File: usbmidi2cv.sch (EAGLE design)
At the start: 33 parts, among them IC1 LM324N

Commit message: melhorias na pcb
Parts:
- R5: device pot:TRIM_EU-B64W -> rcl:R-TRIMM3006P
- renumbered CONTROL_CHANGE to CTRL_CHANGE
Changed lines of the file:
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@@
 <part name="NOTE" library="solpad" library_urn="urn:adsk.eagle:library:364" deviceset="LSP10" device="" package3d_urn="urn:adsk.eagle:package:26501/1"/>
 <part name="SUPPLY4" library="supply2" library_urn="urn:adsk.eagle:library:372" deviceset="GND" device=""/>
-<part name="CONTROL_CHANGE" library="solpad" library_urn="urn:adsk.eagle:library:364" deviceset="LSP10" device="" package3d_urn="urn:adsk.eagle:package:26501/1"/>
+<part name="CTRL_CHANGE" library="solpad" library_urn="urn:adsk.eagle:library:364" deviceset="LSP10" device="" package3d_urn="urn:adsk.eagle:package:26501/1"/>
 <part name="IC1" library="linear" library_urn="urn:adsk.eagle:library:262" deviceset="LM324" device="N" package3d_urn="urn:adsk.eagle:package:16407/2"/>
 <part name="R4" library="rcl" library_urn="urn:adsk.eagle:library:334" deviceset="R-EU_" device="0207/12" package3d_urn="urn:adsk.eagle:package:23489/1" value="10k"/>
 <part name="SUPPLY6" library="supply2" library_urn="urn:adsk.eagle:library:372" deviceset="GND" device=""/>
-<part name="R5" library="pot" library_urn="urn:adsk.eagle:library:331" deviceset="TRIM_EU-" device="B64W" package3d_urn="urn:adsk.eagle:package:22686/1" value="2k"/>
+<part name="R5" library="rcl" library_urn="urn:adsk.eagle:library:334" deviceset="R-TRIMM" device="3006P" package3d_urn="urn:adsk.eagle:package:23758/1" value="2k"/>
 <part name="R6" library="rcl" library_urn="urn:adsk.eagle:library:334" deviceset="R-EU_" device="0207/12" package3d_urn="urn:adsk.eagle:package:23489/1" value="6k8"/>
 <part name="PSU_+12V" library="solpad" library_urn="urn:adsk.eagle:library:364" deviceset="LSP10" device="" package3d_urn="urn:adsk.eagle:package:26501/1"/>
@@
 </instance>
 <instance part="SUPPLY4" gate="GND" x="-25.4" y="68.58" smashed="yes"/>
-<instance part="CONTROL_CHANGE" gate="1" x="55.88" y="-5.08" smashed="yes" rot="R270">
+<instance part="CTRL_CHANGE" gate="1" x="55.88" y="-5.08" smashed="yes" rot="R270">
 <attribute name="NAME" x="59.69" y="-4.699" size="1.778" layer="95"/>
 </instance>
@@
 </instance>
 <instance part="SUPPLY6" gate="GND" x="30.48" y="30.48" smashed="yes"/>
-<instance part="R5" gate="1" x="35.56" y="38.1" smashed="yes" rot="R90">
+<instance part="R5" gate="G$1" x="35.56" y="38.1" smashed="yes" rot="R90">
 <attribute name="VALUE" x="36.83" y="34.29" size="1.778" layer="96" rot="R180"/>
 </instance>
@@
 <segment>
 <pinref part="IC1" gate="D" pin="OUT"/>
-<pinref part="CONTROL_CHANGE" gate="1" pin="MP"/>
+<pinref part="CTRL_CHANGE" gate="1" pin="MP"/>
 <wire x1="17.78" y1="-5.08" x2="20.32" y2="-5.08" width="0.1524" layer="91"/>
 <wire x1="20.32" y1="-5.08" x2="53.34" y2="-5.08" width="0.1524" layer="91"/>
@@
 <pinref part="NOTE" gate="1" pin="MP"/>
 <wire x1="17.78" y1="45.72" x2="35.56" y2="45.72" width="0.1524" layer="91"/>
-<pinref part="R5" gate="1" pin="S"/>
+<pinref part="R5" gate="G$1" pin="S"/>
 <wire x1="35.56" y1="45.72" x2="53.34" y2="45.72" width="0.1524" layer="91"/>
 <wire x1="35.56" y1="43.18" x2="35.56" y2="45.72" width="0.1524" layer="91"/>
@@
 <segment>
 <pinref part="R6" gate="G$1" pin="2"/>
-<pinref part="R5" gate="1" pin="E"/>
-</segment>
-</net>
+<pinref part="R5" gate="G$1" pin="E"/>
+</segment>
+</net>

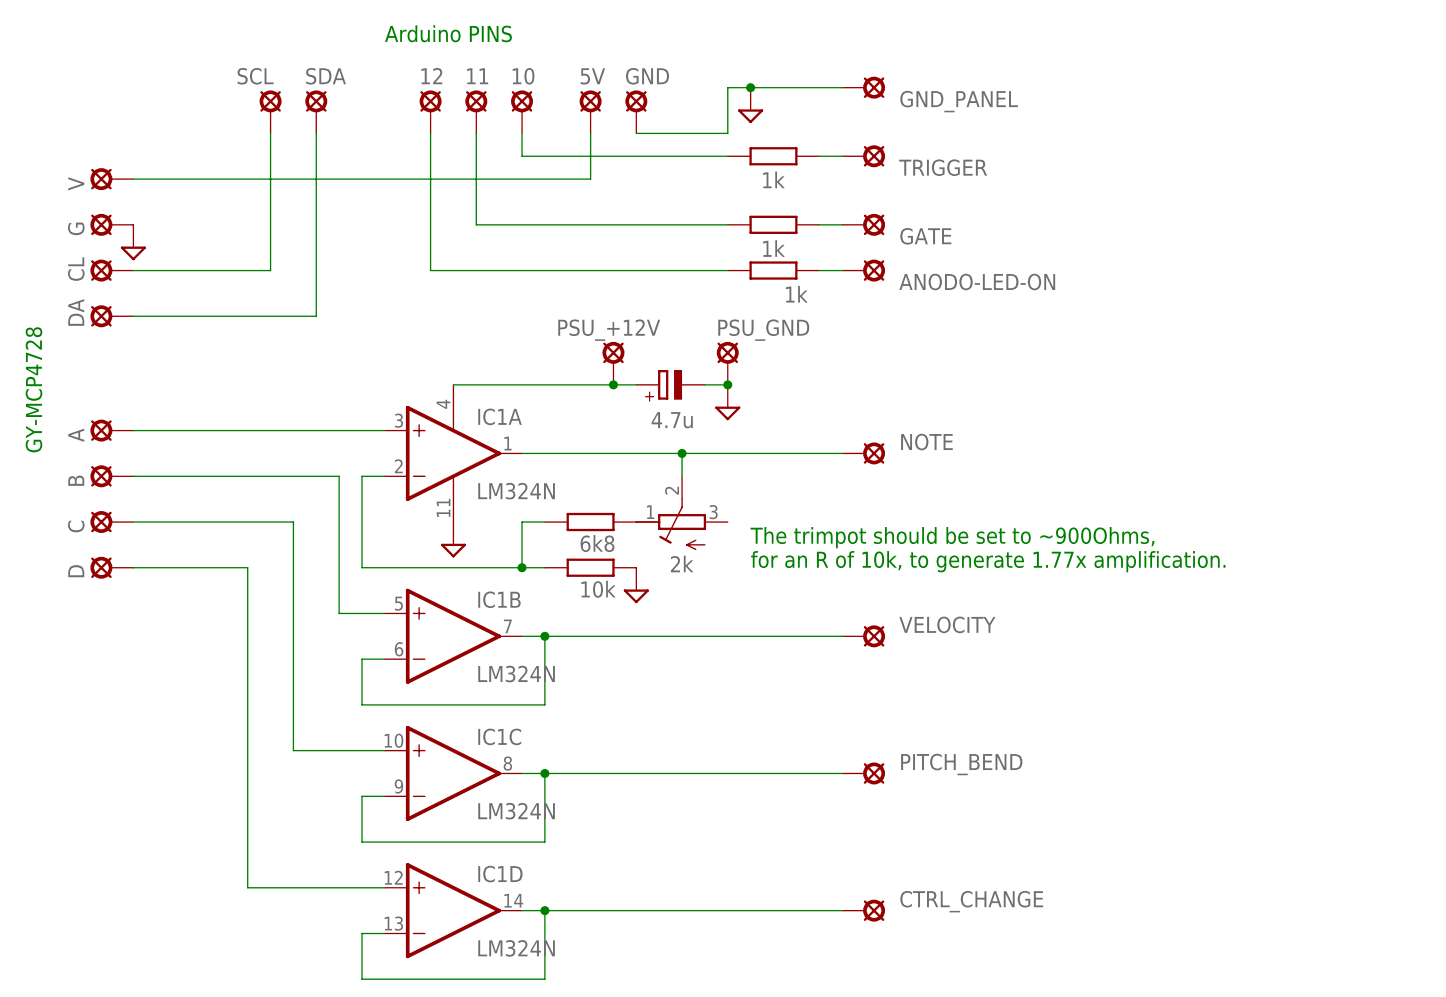
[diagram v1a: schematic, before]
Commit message: change soldpad size
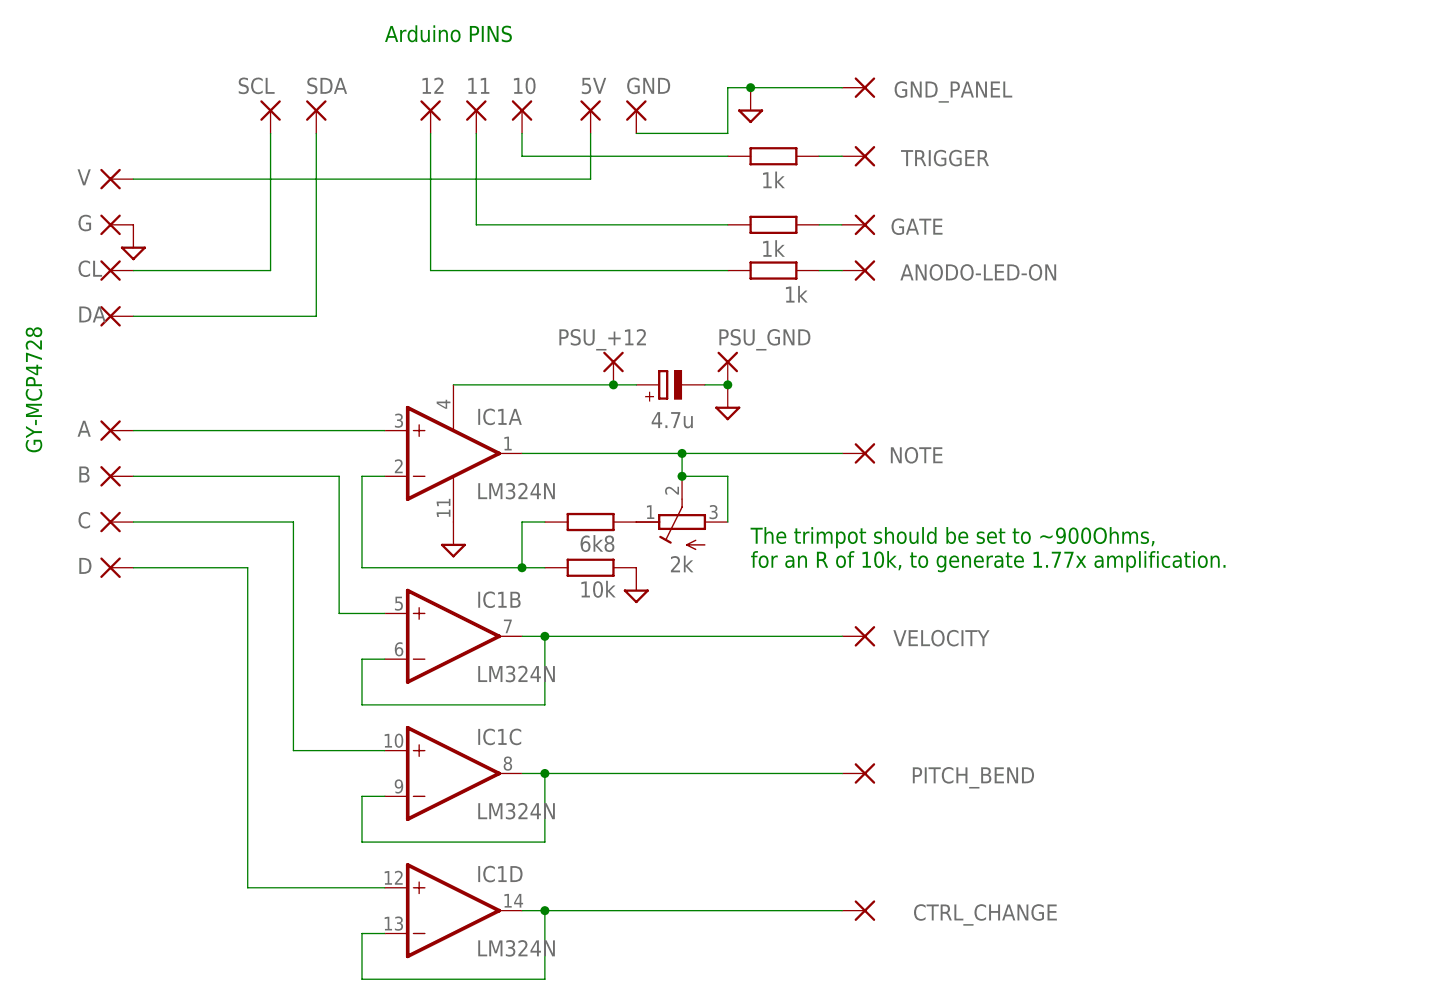
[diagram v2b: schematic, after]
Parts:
- removed PSU_+12V: LSP10, solpad:LSP10
- added PSU_+12: (no value), wirepad:1,6/0,8
- 10, 11, 12, 5V, A, ANODO-LED-ON, B, C, CL, CTRL_CHANGE, D, DA, G, GATE, GND, GND_PANEL, NOTE, PITCH_BEND, PSU_GND, SCL, SDA, TRIGGER, V, VELOCITY: value LSP10 -> (none); device solpad:LSP10 -> wirepad:1,6/0,8
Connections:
- net GND: now also G.P, GND.P, GND_PANEL.P, PSU_GND.P; no longer G.MP, GND.MP, GND_PANEL.MP, PSU_GND.MP
- net N$1: now also A.P; no longer A.MP
- net N$10: now also DA.P, SDA.P; no longer DA.MP, SDA.MP
- net N$11: now also B.P; no longer B.MP
- net N$12: now also C.P; no longer C.MP
- net N$13: now also CTRL_CHANGE.P; no longer CTRL_CHANGE.MP
- net N$14: now also NOTE.P, R5.A; no longer NOTE.MP
- net N$15: now also PITCH_BEND.P; no longer PITCH_BEND.MP
- net N$16: now also VELOCITY.P; no longer VELOCITY.MP
- net N$19: now also PSU_+12.P; no longer PSU_+12V.MP
- net N$2: now also TRIGGER.P; no longer TRIGGER.MP
- net N$20: now also D.P; no longer D.MP
- net N$3: now also GATE.P; no longer GATE.MP
- net N$4: now also 10.P; no longer 10.MP
- net N$5: now also 11.P; no longer 11.MP
- net N$6: now also ANODO-LED-ON.P; no longer ANODO-LED-ON.MP
- net N$7: now also 12.P; no longer 12.MP
- net N$8: now also 5V.P, V.P; no longer 5V.MP, V.MP
- net N$9: now also CL.P, SCL.P; no longer CL.MP, SCL.MP
